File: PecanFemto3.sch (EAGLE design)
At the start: 50 parts, among them IC1 SPV1040T, IC3 EVA7M, IC4 SI4060/3, IC5 LPC824M201JHI33E, U1 TPS62203DBVT

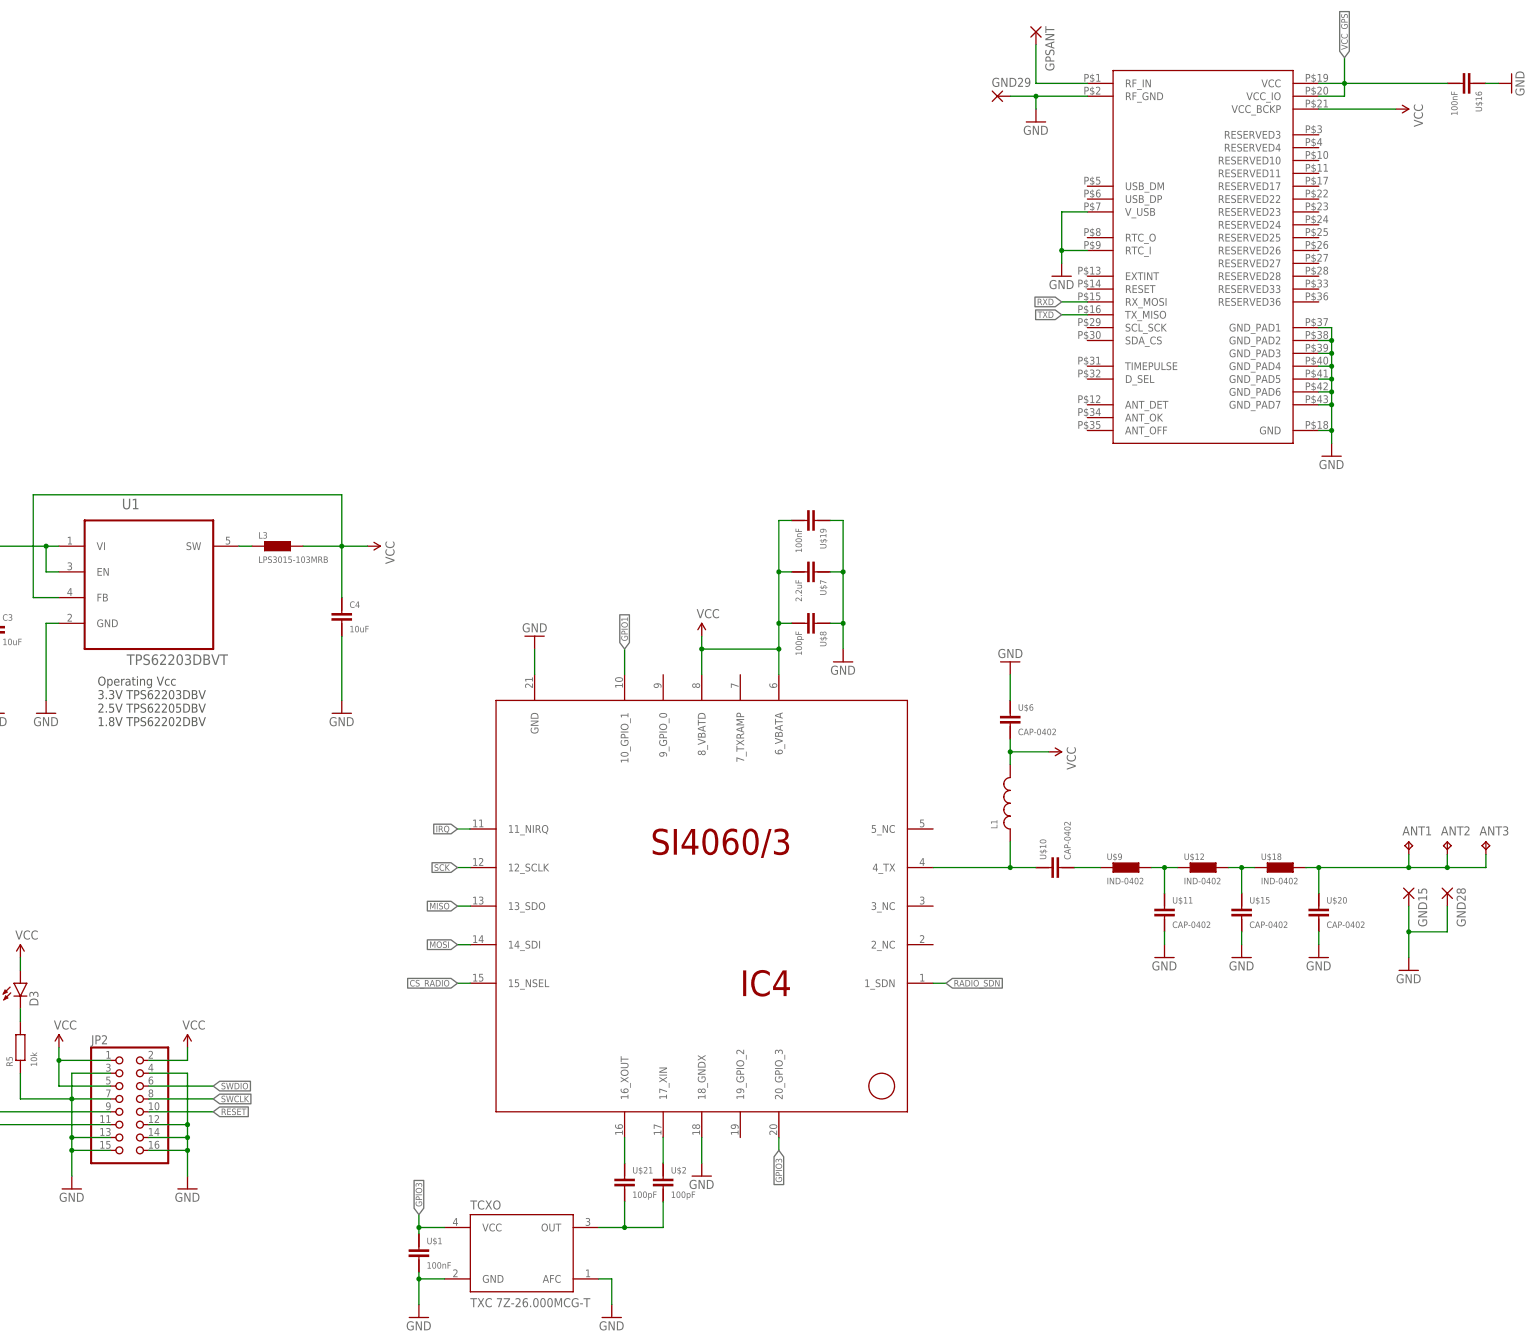
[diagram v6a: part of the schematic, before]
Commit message: Changed naming of parts
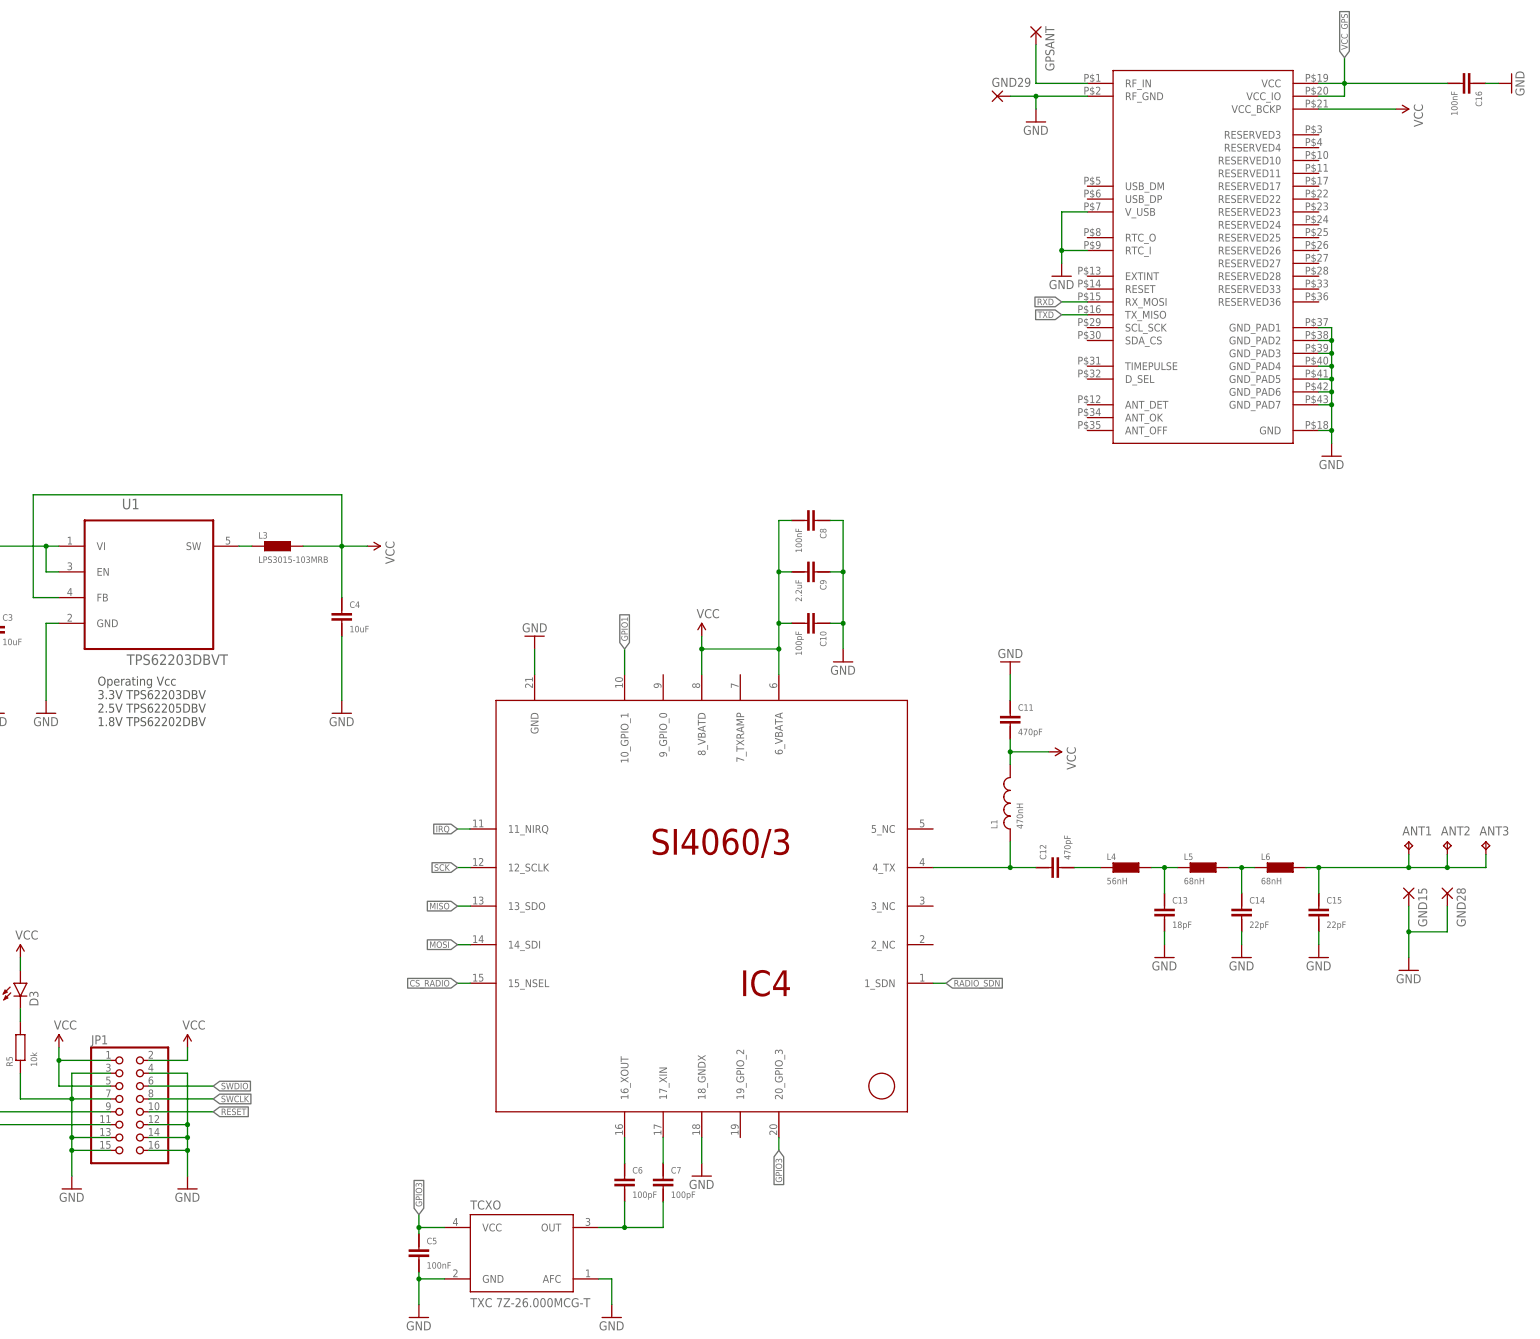
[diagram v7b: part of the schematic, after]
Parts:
- C11, C12: value CAP-0402 -> 470pF
- C13: value CAP-0402 -> 18pF
- C14, C15: value CAP-0402 -> 22pF
- L1: value (none) -> 470nH
- L4: value IND-0402 -> 56nH
- L5, L6: value IND-0402 -> 68nH
- renumbered JP2 to JP1, U$1 to C5, U$10 to C12, U$11 to C13, U$12 to L5, U$15 to C14, U$16 to C16, U$18 to L6, U$19 to C8, U$2 to C7, U$20 to C15, U$21 to C6, U$6 to C11, U$7 to C9, U$8 to C10, U$9 to L4
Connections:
- net N$4 renamed C12
- net N$5 renamed L5

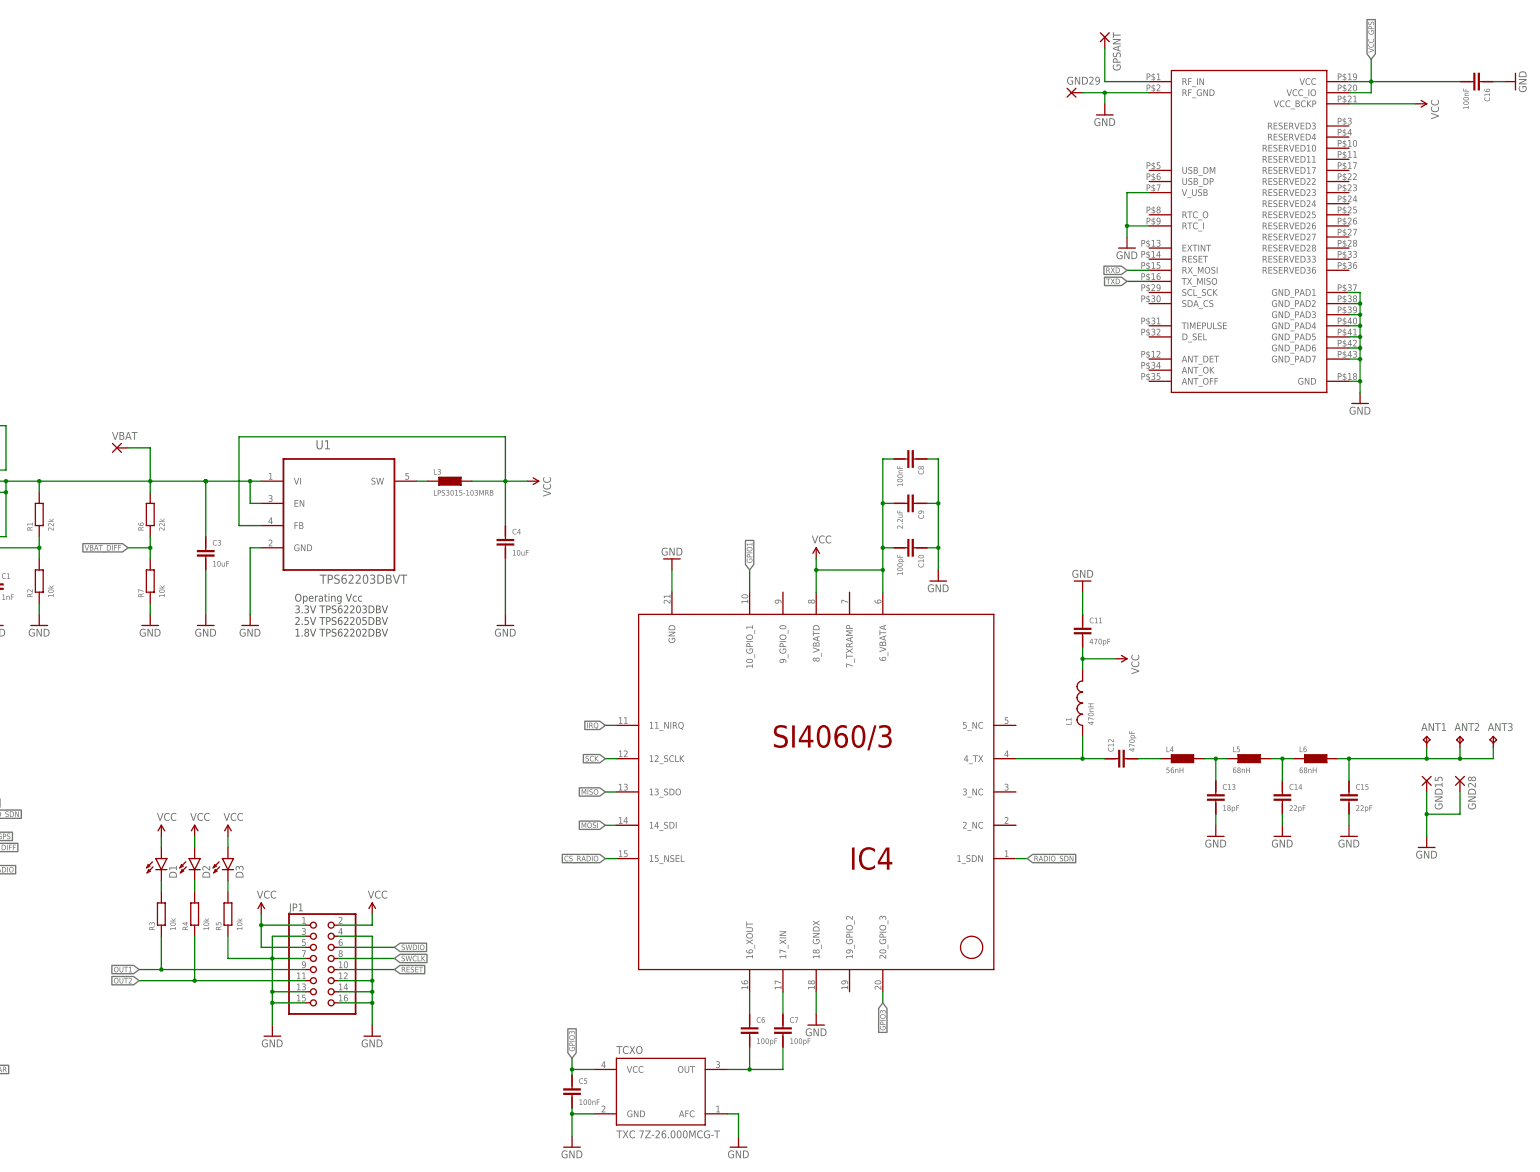
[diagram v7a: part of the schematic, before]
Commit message: Moved parts in schematic, added PNG files
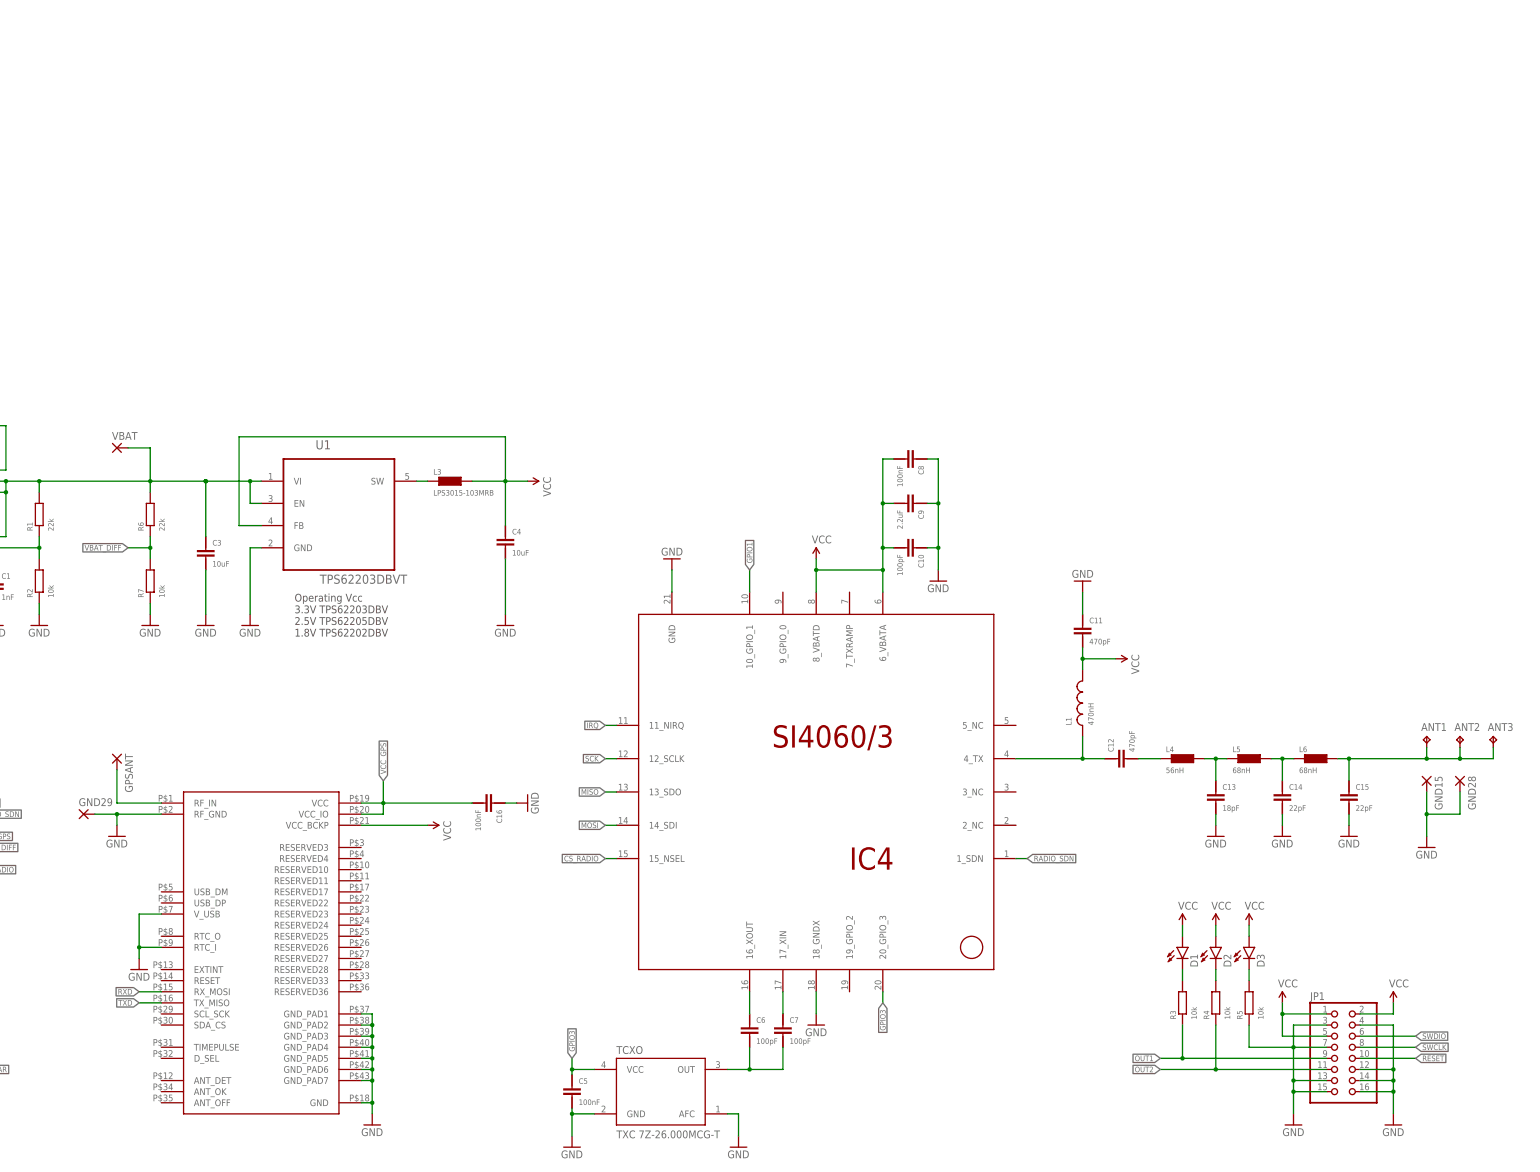
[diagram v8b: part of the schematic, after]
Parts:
- ANT1, ANT2, ANT3: MPN (none) -> ERJ-3EKF62R0V; OC_NEWARK (none) -> 53W4658
- C1, C10, C11, C12, C13, C14, C15, C16, C2, C3, C4, C5, C6, C7, C8, C9, D1, D2, D3, GND15, GND24, GND28, GND29, GND30, GPSANT, IC1, IC3, IC4, IC5, JP1, L1, L2, L3, L4, L5, L6, R1, R2, R3, R4, R5, R6, R7, TCXO, VBAT, VSOL: OC_NEWARK (none) -> unknown
- U1: MF (none) -> TEXAS INSTRUMENTS
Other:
- moved on the sheet: C16, D1, D2, D3, GND29, GPSANT, JP1, R3, R4, R5
